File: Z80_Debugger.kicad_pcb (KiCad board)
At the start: 2 copper layers, 84 x 84 mm, 28 parts, among them J1 ICSP, J2 UART, J3 I2C, J4 microSD, J5 CLK_SW, J6 M1_O, J7 USB_B_Mini, U1 Z84C00_PLCC, U2 PIC18F4520-xP, U3 AS6C4008-55PCN, U4 74HC138, U5 74AHC273, Y1 CXO_DIP14, Y2 Crystal

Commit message: Rev1.1: Fix PUll-UPs pins
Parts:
- added R5: 10K, Resistor_THT:R_Axial_DIN0207_L6.3mm_D2.5mm_P10.16mm_Horizontal, F.Cu at (142.0, 120.5)
- added R7: 10K, Resistor_THT:R_Axial_DIN0207_L6.3mm_D2.5mm_P10.16mm_Horizontal, F.Cu at (148.0, 120.4)
- added R8: 10K, Resistor_THT:R_Axial_DIN0207_L6.3mm_D2.5mm_P10.16mm_Horizontal, F.Cu at (145.0, 120.5)
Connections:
- R4 pad 2: GND -> VCC
- R6 pad 2: GND -> VCC
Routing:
- net /INT: track 32.2 -> 130.5 mm, vias 3 -> 8
- net /BUSREQ: track 33.8 -> 102.6 mm, vias 4 -> 16
- net /RESET: track 72.7 -> 84.4 mm, vias 7 -> 10
- net /D1: track 115.7 -> 119.0 mm, vias 5 -> 7
- net /D6: track 81.5 -> 84.8 mm
- net /D0: track 133.2 -> 136.0 mm, vias 10 -> 12
- net /0x81: track 51.9 -> 54.3 mm
- net /MCLR: track 75.3 -> 77.3 mm
- net /0x82: track 58.9 -> 60.5 mm
- net /PIC_CLK: track 35.7 -> 37.2 mm
- net /A18: track 53.8 -> 54.4 mm
- net /TX: track 71.8 -> 72.1 mm, vias 0 -> 2
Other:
- board text added: "Z80-Debugger Rev.1.1 @ 27.07.26 @deulamco"
- board text removed: "Z80-Debugger Rev.1 @ 27.07.26 @deulamco"

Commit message: Refine SPI/MicroSD pins.
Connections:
- net /SDI renamed /MOSI
- net /SDO renamed /MISO
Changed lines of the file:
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@@
 			(layers "*.Cu" "*.Mask")
 			(remove_unused_layers no)
-			(net "/SDI")
+			(net "/MOSI")
 			(pinfunction "RA2_4")
 			(pintype "bidirectional")
@@
 			(layers "*.Cu" "*.Mask")
 			(remove_unused_layers no)
-			(net "/SDO")
+			(net "/MISO")
 			(pinfunction "RA3_5")
 			(pintype "bidirectional")
@@
 			(layers "*.Cu" "*.Mask")
 			(remove_unused_layers no)
-			(net "/SDI")
+			(net "/MOSI")
 			(pinfunction "Pin_3_3")
 			(pintype "passive")
@@
 			(layers "*.Cu" "*.Mask")
 			(remove_unused_layers no)
-			(net "/SDO")
+			(net "/MISO")
 			(pinfunction "Pin_4_4")
 			(pintype "passive")
@@
 		(width 0.2)
 		(layer "F.Cu")
-		(net "/SDI")
+		(net "/MOSI")
 	)
 	(segment
@@
 		(width 0.2)
 		(layer "F.Cu")
-		(net "/SDI")
+		(net "/MOSI")
 	)
 	(segment
@@
 		(width 0.2)
 		(layer "F.Cu")
-		(net "/SDI")
+		(net "/MOSI")
 	)
 	(segment
@@
 		(width 0.2)
 		(layer "F.Cu")
-		(net "/SDI")
+		(net "/MOSI")
 	)
 	(segment
@@
 		(width 0.2)
 		(layer "F.Cu")
-		(net "/SDI")
+		(net "/MOSI")
 	)
 	(segment
@@
 		(width 0.2)
 		(layer "F.Cu")
-		(net "/SDO")
+		(net "/MISO")
 	)
 	(segment
@@
 		(width 0.2)
 		(layer "F.Cu")
-		(net "/SDO")
+		(net "/MISO")
 	)
 	(segment
@@
 		(width 0.2)
 		(layer "F.Cu")
-		(net "/SDO")
+		(net "/MISO")
 	)
 	(segment
@@
 		(width 0.2)
 		(layer "F.Cu")
-		(net "/SDO")
+		(net "/MISO")
 	)
 	(segment
@@
 		(width 0.2)
 		(layer "F.Cu")
-		(net "/SDO")
+		(net "/MISO")
 	)
 	(segment
@@
 		(width 0.2)
 		(layer "F.Cu")
-		(net "/SDO")
+		(net "/MISO")
 	)
 	(segment
@@
 		(width 0.2)
 		(layer "F.Cu")
-		(net "/SDO")
+		(net "/MISO")
 	)
 	(segment
@@
 		(width 0.2)
 		(layer "F.Cu")
-		(net "/SDO")
+		(net "/MISO")
 	)
 	(segment

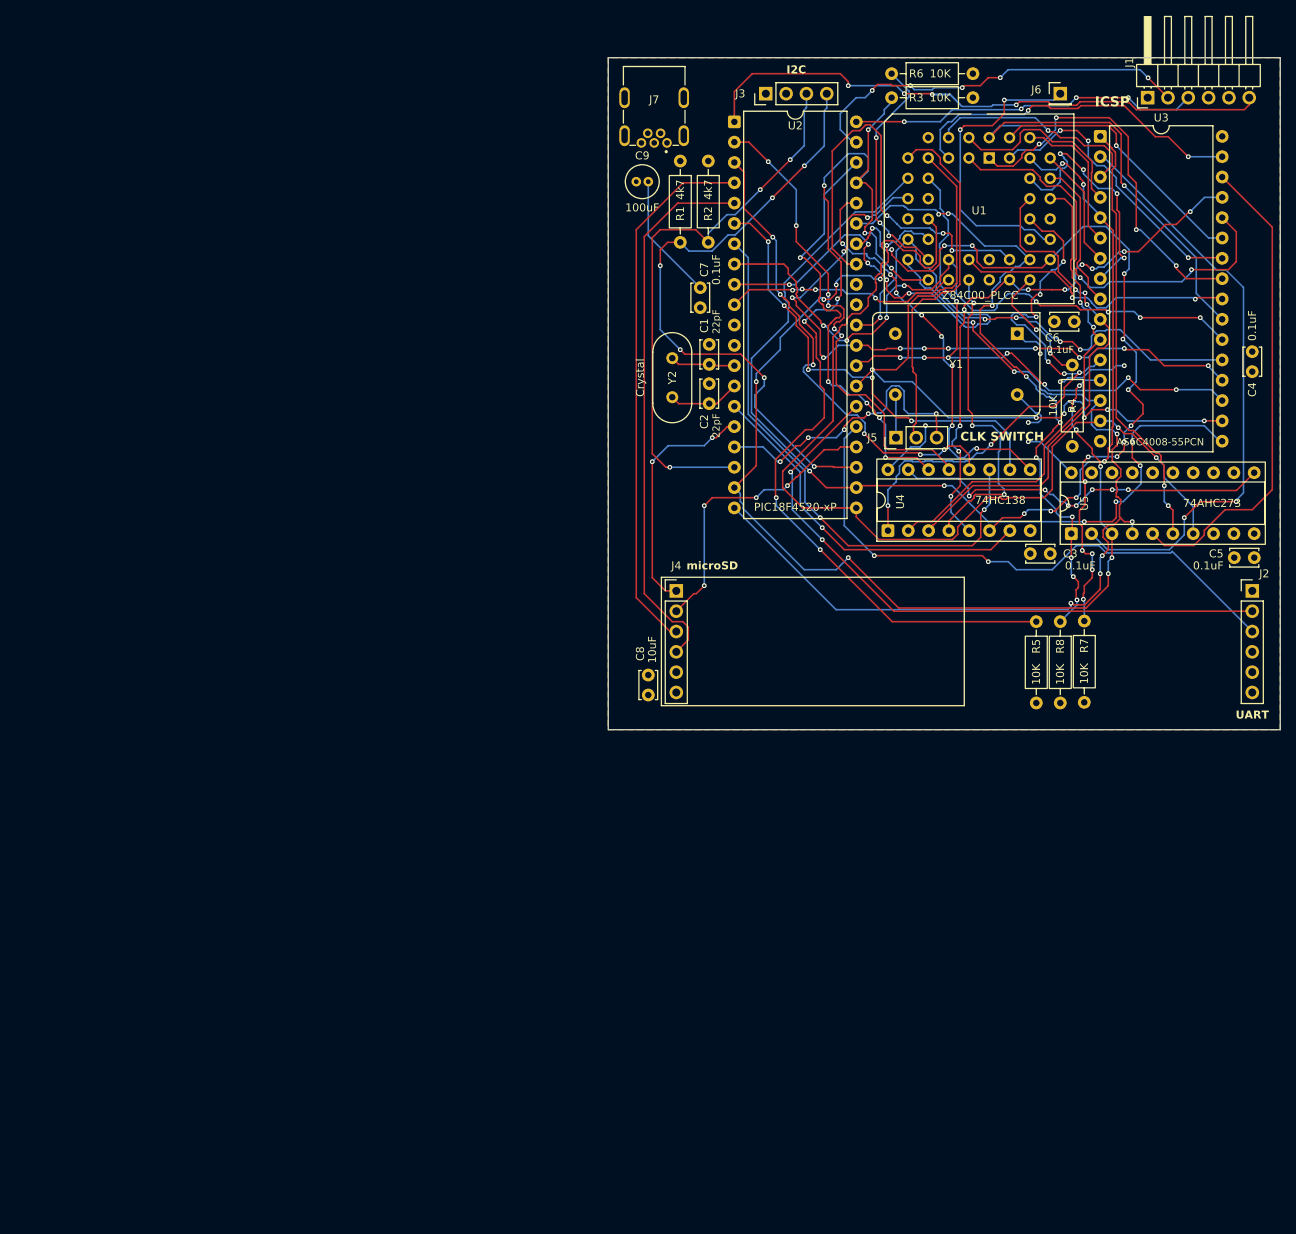
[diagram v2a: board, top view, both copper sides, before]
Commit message: Rev.2: adding 3x74HC595
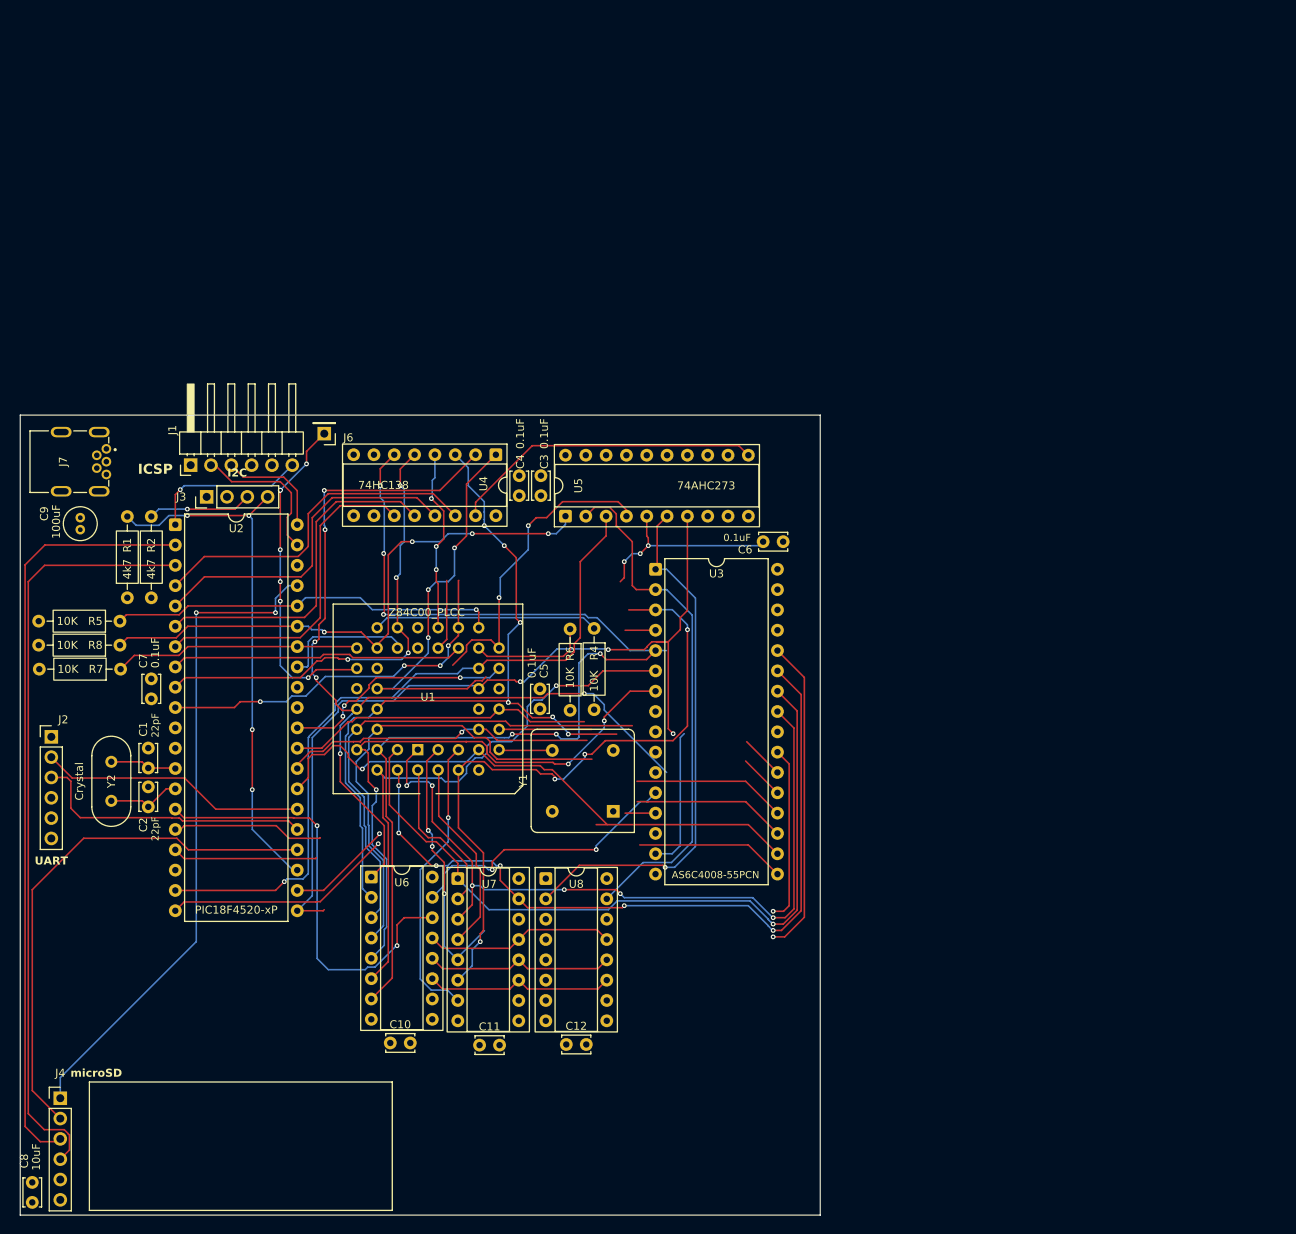
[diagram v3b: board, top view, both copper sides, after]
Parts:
- removed J5: CLK_SW, Connector_PinHeader_2.54mm:PinHeader_1x03_P2.54mm_Vertical
- removed R3: 10K, Resistor_THT:R_Axial_DIN0207_L6.3mm_D2.5mm_P10.16mm_Horizontal
- added C10: 0.1uF, Capacitor_THT:C_Disc_D3.4mm_W2.1mm_P2.50mm, F.Cu at (61.2, 173.2)
- added C11: 0.1uF, Capacitor_THT:C_Disc_D3.4mm_W2.1mm_P2.50mm, F.Cu at (72.4, 173.4)
- added C12: 0.1uF, Capacitor_THT:C_Disc_D3.4mm_W2.1mm_P2.50mm, F.Cu at (83.2, 173.3)
- added U6: 74HC595, Package_DIP:DIP-16_W7.62mm_Socket, F.Cu at (58.9, 152.4)
- added U7: 74HC595, Package_DIP:DIP-16_W7.62mm_Socket, F.Cu at (69.7, 152.6)
- added U8: 74HC595, Package_DIP:DIP-16_W7.62mm_Socket, F.Cu at (80.7, 152.6)
- Y1: value CXO_DIP14 -> CXO_DIP8; footprint Oscillator:Oscillator_DIP-14 -> Oscillator:Oscillator_DIP-8
- moved J2 151.2 mm to (18.9, 134.9)
- moved J1 128.1 mm to (36.3, 100.9)
- moved R7 120.6 mm to (27.5, 126.4), turned to 180 degrees
- moved R8 117.6 mm to (27.5, 123.4), turned to 180 degrees
- moved R5 114.5 mm to (27.5, 120.4), turned to 180 degrees
- moved U1 102.8 mm to (64.7, 136.5), turned to 180 degrees
- moved J6 101.3 mm to (53.0, 97.0), turned to 180 degrees
- moved C8 99.8 mm to (16.5, 193.1)
- moved J4 99.8 mm to (20.0, 180.1)
- moved C4 92.9 mm to (77.4, 104.8)
- moved C5 91.3 mm to (80.0, 131.4), turned to 90 degrees
- moved R2 88.5 mm to (31.4, 117.5), turned to 90 degrees
- moved R1 88.1 mm to (28.4, 117.5), turned to 90 degrees
- moved Y2 86.4 mm to (26.4, 142.9)
- moved C1 86.4 mm to (31.0, 138.8)
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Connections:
- U2 pad 15: /0x87 -> /SER
- U2 pad 16: /CS -> /SRCLK
- U2 pad 17: /PIC_CLK -> /RCLK
- U2 pad 2: /0x82 -> /MOSI
- U2 pad 3: /0x83 -> /MISO
- U2 pad 36: /0x86 -> /INT
- U2 pad 37: /INT -> /CS
- U2 pad 38: /0x81 -> /595E
- U2 pad 4: /MOSI -> /0x81
- U2 pad 5: /MISO -> /0x82
- U2 pad 6: /0x85 -> /0x83
- U4 pad 10: /0x85 -> unconnected-(U4-~{Y5}-Pad10)
- U4 pad 7: /0x87 -> unconnected-(U4-~{Y7}-Pad7)
- U4 pad 9: /0x86 -> unconnected-(U4-~{Y6}-Pad9)
- Y1 pad 8: /20M_CLK -> VCC
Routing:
- net /INT: track 130.5 -> 49.1 mm, vias 8 -> 1
- net /D3: track 116.3 -> 43.6 mm, vias 6 -> 1
- net /A7: track 65.5 -> 137.8 mm
- net /BUSREQ: track 102.6 -> 30.8 mm, vias 16 -> 0
- net /A8: track 33.9 -> 97.3 mm, vias 1 -> 6
- net /A1: track 61.1 -> 121.8 mm, vias 2 -> 6
- net /WR: track 117.8 -> 57.9 mm, vias 15 -> 4
- net /A9: track 37.0 -> 95.6 mm, vias 3 -> 1
- net /A5: track 15.1 -> 73.4 mm, vias 0 -> 3
- net /MCLR: track 77.3 -> 19.9 mm, vias 4 -> 1
- net /0x85: track 57.3 -> 0.00 mm, vias 5 -> 0
- net /SCL: track 70.3 -> 13.0 mm, vias 3 -> 1
- net /A14: track 28.4 -> 82.9 mm, vias 1 -> 4
- net /SER: track 0.00 -> 54.4 mm, vias 0 -> 2
- net /CS: track 30.3 -> 82.8 mm
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- removed copper zone on B.Cu, net GND
- removed copper zone on F.Cu, net VCC
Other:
- board size 84 x 84 mm -> 100 x 100 mm
- board text removed: "CLK SWITCH"

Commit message: add pins: M1, RD, WR for Z80 Req
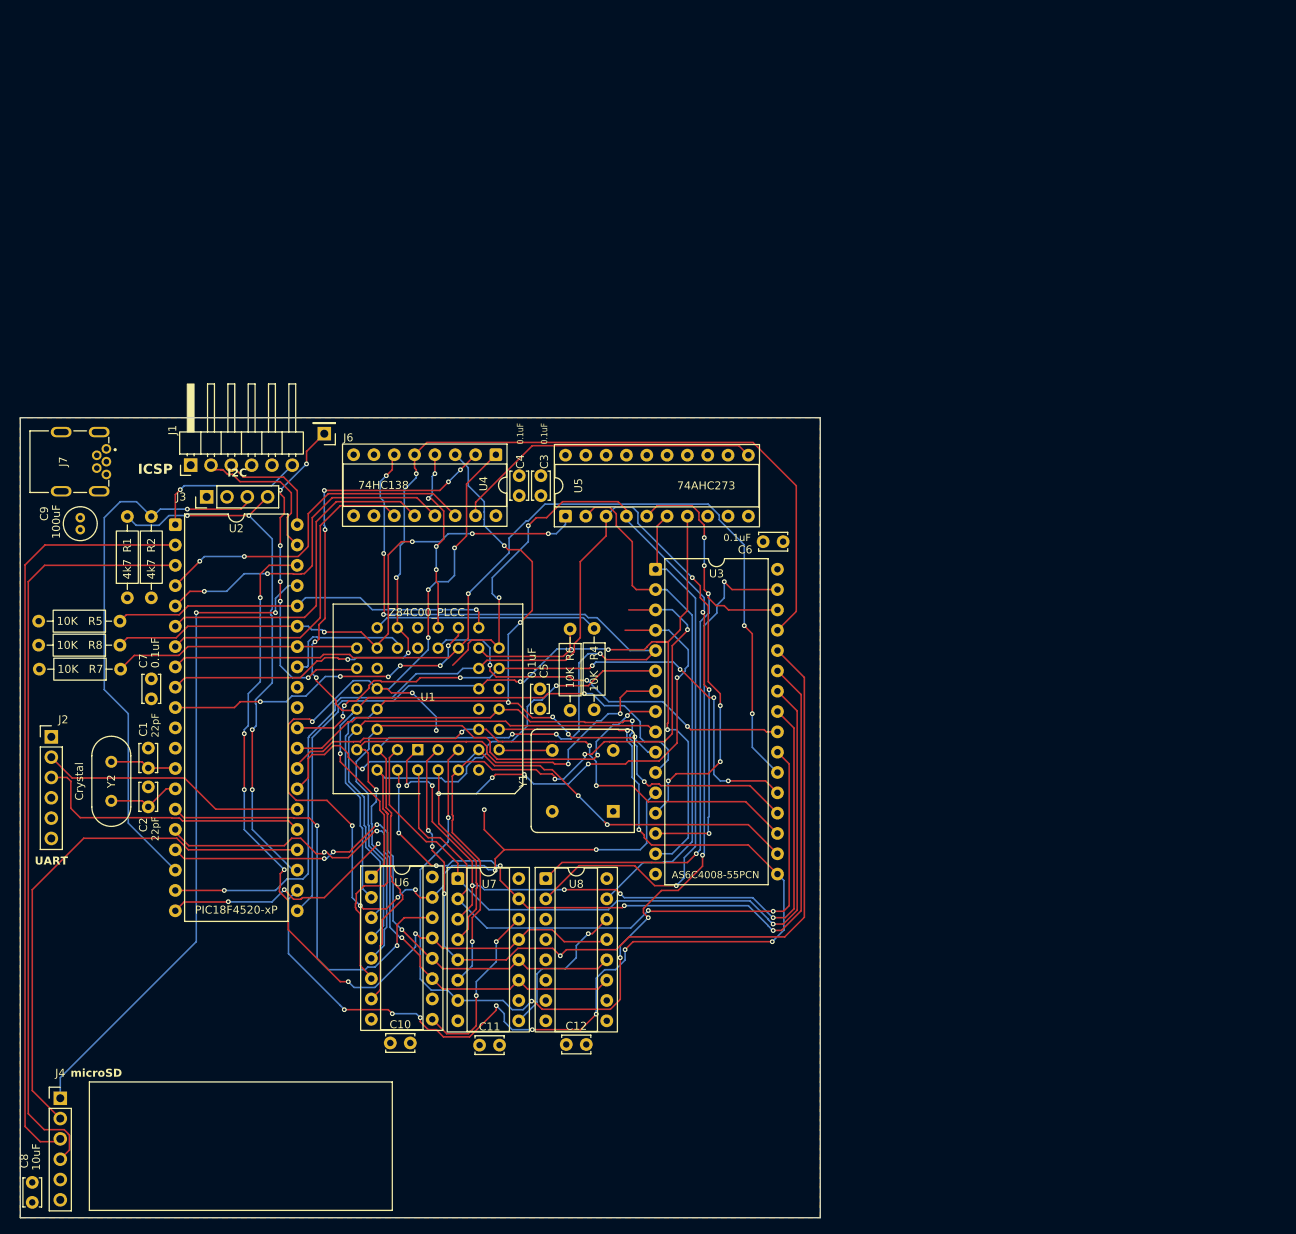
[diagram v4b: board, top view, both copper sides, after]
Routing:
- net /D3: track 43.6 -> 143.5 mm, vias 1 -> 10
- net /A15: track 36.4 -> 125.0 mm, vias 1 -> 6
- net /595E: track 23.8 -> 102.1 mm, vias 0 -> 6
- net /MREQ: track 42.1 -> 116.8 mm, vias 0 -> 3
- net /WR: track 57.9 -> 127.3 mm
- net /A0: track 87.3 -> 146.0 mm, vias 5 -> 13
- net /A17: track 24.3 -> 81.2 mm, vias 3 -> 4
- net /SCL: track 13.0 -> 68.7 mm
- net /D1: track 68.7 -> 121.5 mm, vias 3 -> 8
- net /A12: track 28.3 -> 78.9 mm, vias 0 -> 5
- net /D0: track 95.1 -> 143.6 mm, vias 1 -> 5
- net /D7: track 35.2 -> 77.2 mm, vias 3 -> 7
- net /A10: track 42.1 -> 83.9 mm, vias 1 -> 2
- net /RD: track 8.91 -> 49.3 mm, vias 0 -> 3
- net /A13: track 73.1 -> 109.8 mm
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- added copper zone on B.Cu, net GND
- added copper zone on F.Cu, net VCC
